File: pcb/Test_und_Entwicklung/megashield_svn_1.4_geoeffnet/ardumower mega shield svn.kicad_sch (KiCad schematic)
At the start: 21 parts, among them K3 RELAY_2RT, P16 RPI Backup P., P17 RPI Main P., P42 Charger, P43 Battery, P49 MotorStop, Q1 BC847B

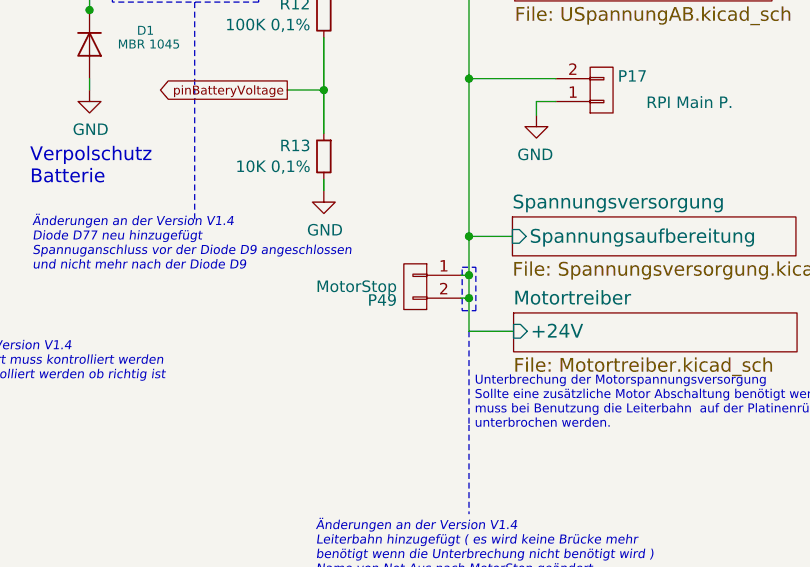
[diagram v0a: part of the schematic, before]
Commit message: megashield_svn_1.4_geoeffnet
megashield_svn_1.4_geoeffnet
23 Dioden und Mosfet unten rechts neu angeordnet
und Motorschutz Klemme von der Rückseite auf die Vorderseite umgeändert
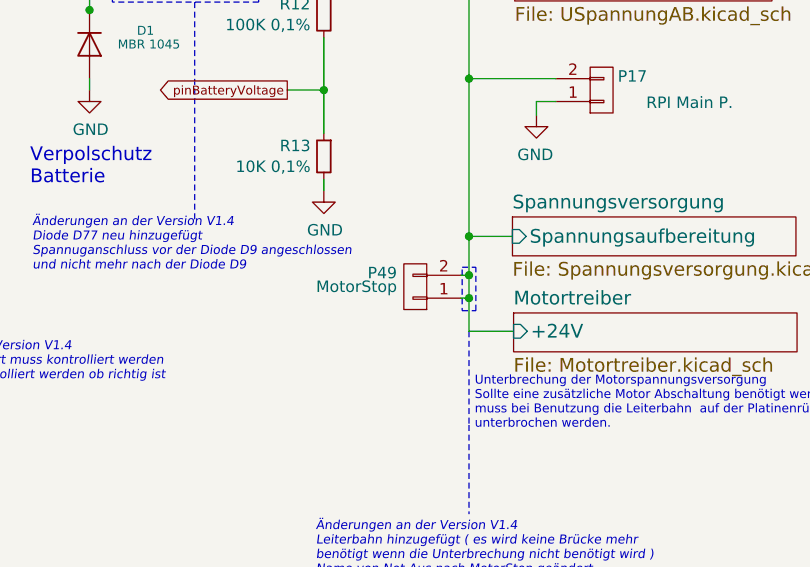
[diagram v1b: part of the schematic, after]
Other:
- moved on the sheet: P49
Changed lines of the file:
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@@
     )
   )
-  (symbol (lib_id "ardumower-mega-shield-svn-rescue:CONN_01X02-RESCUE-ardumower_mega_shield_svn") (at 222.885 99.695 0) (mirror y) (unit 1)
+  (symbol (lib_id "ardumower-mega-shield-svn-rescue:CONN_01X02-RESCUE-ardumower_mega_shield_svn") (at 222.885 99.695 180) (unit 1)
     (in_bom yes) (on_board yes)
-    (property "Reference" "P49" (id 0) (at 220.853 101.219 0)
+    (property "Reference" "P49" (id 0) (at 220.853 98.171 0)
       (effects (font (size 1.27 1.27)) (justify left))
     )
@@
       (effects (font (size 1.27 1.27)) (justify left))
     )
-    (property "Footprint" "Terminal_Blocks:TerminalBlock_Pheonix_MKDS1.5-2pol" (id 2) (at 227.2538 96.4438 90)
+    (property "Footprint" "Terminal_Blocks:TerminalBlock_Pheonix_MKDS1.5-2pol" (id 2) (at 227.2538 102.9462 90)
       (effects (font (size 1.27 1.27)) (justify left) hide)
     )
     (property "Datasheet" "" (id 3) (at 222.885 99.695 0))
-    (property "Gehäuseart" "Value" (id 4) (at 225.7298 96.4438 90)
+    (property "Gehäuseart" "Value" (id 4) (at 225.7298 102.9462 90)
       (effects (font (size 1.524 1.524)) (justify left) hide)
     )
-    (property "Bestelllink" "Value" (id 5) (at 227.076 96.4438 90)
+    (property "Bestelllink" "Value" (id 5) (at 227.076 102.9462 90)
       (effects (font (size 1.524 1.524)) (justify left) hide)
     )
-    (property "Technische Daten" "Value" (id 6) (at 228.4222 96.4438 90)
+    (property "Technische Daten" "Value" (id 6) (at 228.4222 102.9462 90)
       (effects (font (size 1.524 1.524)) (justify left) hide)
     )

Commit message: megashield_svn_1.4_geoeffnet
megashield_svn_1.4_geoeffnet
24 INA Neu verdrahtet und Widerstandswerte von den INA ausgetauscht
Berechnung hinzugefügt
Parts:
- R10, R13: JLCPCB LCSC Part (none) -> C95519
- R12, R9: JLCPCB LCSC Part (none) -> C95527
- R18: JLCPCB LCSC Part (none) -> C4190
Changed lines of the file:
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@@
   (title_block
     (title "Ardumower shield SVN Version")
-    (date "2020-12-30")
+    (date "2021-01-04")
     (rev "1.4")
     (company "ML AG JL UZ")
@@
       (effects (font (size 1.27 1.27)) hide)
     )
+    (property "JLCPCB LCSC Part" "C95527" (id 6) (at 111.76 62.484 0)
+      (effects (font (size 1.27 1.27)) hide)
+    )
   )
   (symbol (lib_id "ardumower-mega-shield-svn-rescue:R_Small-RESCUE-ardumower_mega_shield_svn") (at 111.76 78.232 0) (mirror y) (unit 1)
@@
       (effects (font (size 1.27 1.27)) hide)
     )
+    (property "JLCPCB LCSC Part" "C95519" (id 6) (at 111.76 78.232 0)
+      (effects (font (size 1.27 1.27)) hide)
+    )
   )
   (symbol (lib_id "ardumower-mega-shield-svn-rescue:R_Small-RESCUE-ardumower_mega_shield_svn") (at 133.858 99.568 90) (mirror x) (unit 1)
@@
       (effects (font (size 1.27 1.27)) hide)
     )
+    (property "JLCPCB LCSC Part" "C4190" (id 6) (at 133.858 99.568 0)
+      (effects (font (size 1.27 1.27)) hide)
+    )
   )
   (symbol (lib_id "ardumower-mega-shield-svn-rescue:R_Small-RESCUE-ardumower_mega_shield_svn") (at 212.725 69.469 0) (mirror y) (unit 1)
@@
       (effects (font (size 1.27 1.27)) hide)
     )
+    (property "JLCPCB LCSC Part" "C95527" (id 6) (at 212.725 69.469 0)
+      (effects (font (size 1.27 1.27)) hide)
+    )
   )
   (symbol (lib_id "ardumower-mega-shield-svn-rescue:R_Small-RESCUE-ardumower_mega_shield_svn") (at 212.725 85.217 0) (mirror y) (unit 1)
@@
       (effects (font (size 1.27 1.27)) hide)
     )
+    (property "JLCPCB LCSC Part" "C95519" (id 6) (at 212.725 85.217 0)
+      (effects (font (size 1.27 1.27)) hide)
+    )
   )
   (symbol (lib_id "ardumower-mega-shield-svn-rescue:F_10A-RESCUE-ardumower_mega_shield_svn") (at 52.197 51.816 180) (unit 1)
@@
       (reference "JP16") (unit 1) (value "5A") (footprint "Zimprich:SJ")
     )
-    (path "/882f13dd-ef74-41f9-a374-92f084b19f4e/00000000-0000-0000-0000-0000587a79b6"
-      (reference "R138") (unit 1) (value "10K") (footprint "Zimprich:R_0603")
-    )
     (path "/882f13dd-ef74-41f9-a374-92f084b19f4e/00000000-0000-0000-0000-0000587a6b3f"
-      (reference "R139") (unit 1) (value "10K") (footprint "Zimprich:R_0603")
+      (reference "R138") (unit 1) (value "6,80K") (footprint "Zimprich:R_0603")
+    )
+    (path "/882f13dd-ef74-41f9-a374-92f084b19f4e/00000000-0000-0000-0000-0000587a79b6"
+      (reference "R139") (unit 1) (value "3,30K") (footprint "Zimprich:R_0603")
     )
     (path "/882f13dd-ef74-41f9-a374-92f084b19f4e/00000000-0000-0000-0000-0000587a7cc4"
-      (reference "R140") (unit 1) (value "0.1 1% 2W") (footprint "Resistor_SMD:R_2512_6332Metric")
+      (reference "R140") (unit 1) (value "0.05 1% 2W") (footprint "Resistor_SMD:R_2512_6332Metric")
     )
   )

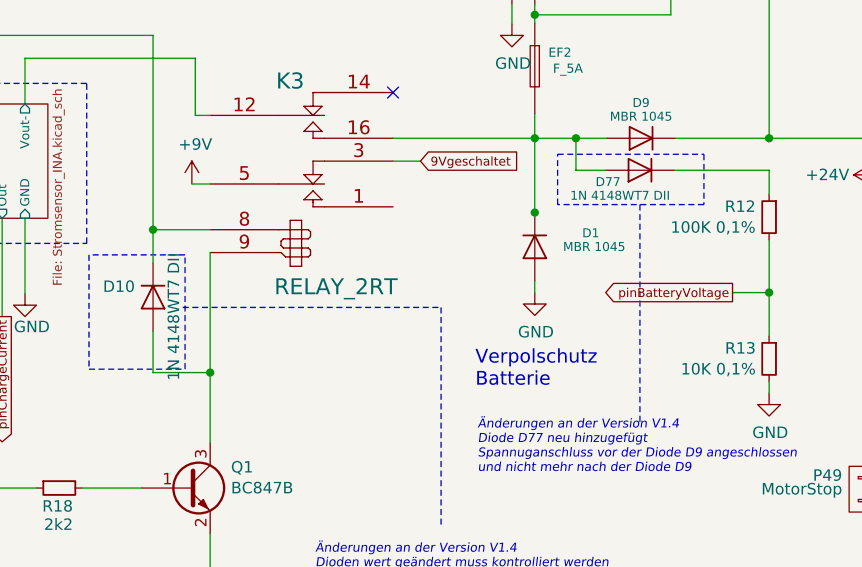
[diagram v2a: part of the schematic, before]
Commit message: megashield_svn_1.4_geoeffnet
megashield_svn_1.4_geoeffnet
26 Diode D10&D77 von Footprint SOD-523 auf SOD-123 & auf 1N4148W geändert
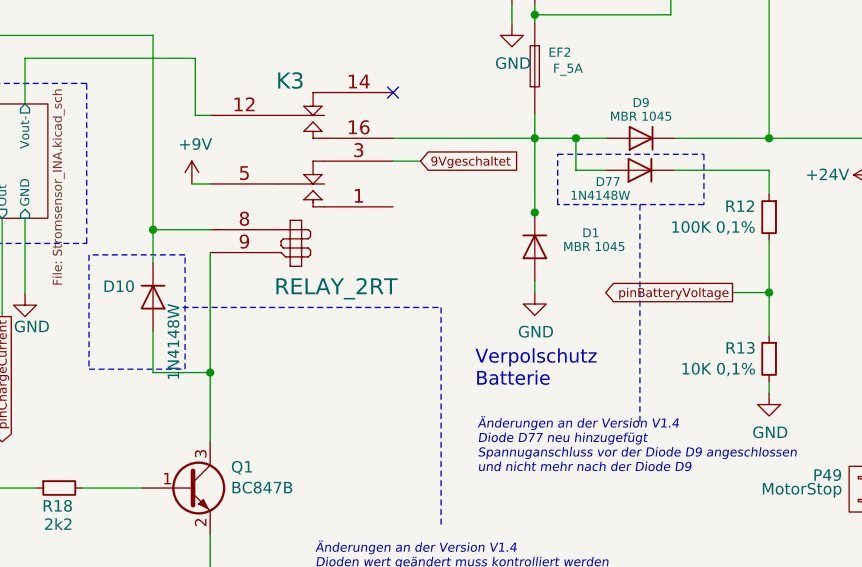
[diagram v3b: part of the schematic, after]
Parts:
- D10: value 1N 4148WT7 DII -> 1N4148W; footprint Diode_SMD:D_SOD-523 -> Diode_SMD:D_SOD-123; Bauform SOD-523 -> SOD-123; Bestelllink https://www.reichelt.de/schalt-diode-100-v-150-ma-sod-523-1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 -> https://www.reichelt.de/schalt-diode-75-v-150-ma-sod-123-rn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; Bestellnummer R: 1N 4148WT7 DII -> R: RND 1N4148W; Funktion Schalt-Diode, 100 V, 150 mA, SOD-523 -> Schalt-Diode, 75 V, 150 mA, SOD-123; Gehäuseart SOD-523 -> SOD-123; Reichelt-Bestellnummer R: 1N 4148WT7 DII -> R: RND 1N4148W; Technische Daten Schalt-Diode, 100 V, 150 mA, SOD-523 -> Schalt-Diode, 75 V, 150 mA, SOD-123
- D77: value 1N 4148WT7 DII -> 1N4148W; footprint Diode_SMD:D_SOD-523 -> Diode_SMD:D_SOD-123; Bauform SOD-523 -> SOD-123; Bestelllink https://www.reichelt.de/schalt-diode-100-v-150-ma-sod-523-1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 -> https://www.reichelt.de/schalt-diode-75-v-150-ma-sod-123-rn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; Bestellnummer R: 1N 4148WT7 DII -> R: RND 1N4148W; Funktion Schalt-Diode, 100 V, 150 mA, SOD-523 -> Schalt-Diode, 75 V, 150 mA, SOD-123; Gehäuseart SOD-523 -> SOD-123; Hersteller Bestellnummer Value -> (none); Reichelt-Bestellnummer R: 1N 4148WT7 DII -> R: RND 1N4148W; Technische Daten Schalt-Diode, 100 V, 150 mA, SOD-523 -> Schalt-Diode, 75 V, 150 mA, SOD-123
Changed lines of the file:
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@@
   (title_block
     (title "Ardumower shield SVN Version")
-    (date "2021-01-04")
+    (date "2021-01-06")
     (rev "1.4")
     (company "ML AG JL UZ")
@@
       (effects (font (size 1.27 1.27)) (justify right))
     )
-    (property "Value" "1N 4148WT7 DII" (id 1) (at 146.5834 87.63 0)
+    (property "Value" "1N4148W" (id 1) (at 146.5834 87.63 0)
       (effects (font (size 1.27 1.27)) (justify right))
     )
-    (property "Footprint" "Diode_SMD:D_SOD-523" (id 2) (at 139.827 78.359 0)
-      (effects (font (size 1.27 1.27)) hide)
-    )
-    (property "Datasheet" "https://cdn-reichelt.de/documents/datenblatt/A400/1N4148WT_ENG_TDS.pdf" (id 3) (at 144.272 78.359 0)
-      (effects (font (size 1.27 1.27)) hide)
-    )
-    (property "Bauform" "SOD-523" (id 4) (at 144.272 78.359 0)
-      (effects (font (size 1.27 1.27)) hide)
-    )
-    (property "Bestelllink" "https://www.reichelt.de/schalt-diode-100-v-150-ma-sod-523-1n-4148wt7-dii-p219386.html?&trstct=pos_6&nbc=1" (id 5) (at 144.272 78.359 0)
-      (effects (font (size 1.27 1.27)) hide)
-    )
-    (property "Technische Daten" "Schalt-Diode, 100 V, 150 mA, SOD-523" (id 6) (at 144.272 78.359 0)
-      (effects (font (size 1.27 1.27)) hide)
-    )
-    (property "Bestellnummer" "R: 1N 4148WT7 DII" (id 7) (at 144.272 78.359 0)
-      (effects (font (size 1.27 1.27)) hide)
-    )
-    (property "Funktion" "Schalt-Diode, 100 V, 150 mA, SOD-523" (id 4) (at 144.272 78.359 0)
-      (effects (font (size 1.27 1.27)) hide)
-    )
-    (property "Gehäuseart" "SOD-523" (id 5) (at 144.272 78.359 0)
-      (effects (font (size 1.27 1.27)) hide)
-    )
-    (property "Reichelt-Bestellnummer" "R: 1N 4148WT7 DII" (id 6) (at 144.272 78.359 0)
+    (property "Footprint" "Diode_SMD:D_SOD-123" (id 2) (at 139.827 78.359 0)
+      (effects (font (size 1.27 1.27)) hide)
+    )
+    (property "Datasheet" "https://cdn-reichelt.de/documents/datenblatt/A200/RND_1N4148W_DB-EN.pdf" (id 3) (at 144.272 78.359 0)
+      (effects (font (size 1.27 1.27)) hide)
+    )
+    (property "Bauform" "SOD-123" (id 4) (at 144.272 78.359 0)
+      (effects (font (size 1.27 1.27)) hide)
+    )
+    (property "Bestelllink" "https://www.reichelt.de/schalt-diode-75-v-150-ma-sod-123-rnd-1n4148w-p223369.html?&trstct=pos_0&nbc=1" (id 5) (at 144.272 78.359 0)
+      (effects (font (size 1.27 1.27)) hide)
+    )
+    (property "Technische Daten" "Schalt-Diode, 75 V, 150 mA, SOD-123" (id 6) (at 144.272 78.359 0)
+      (effects (font (size 1.27 1.27)) hide)
+    )
+    (property "Bestellnummer" "R: RND 1N4148W" (id 7) (at 144.272 78.359 0)
+      (effects (font (size 1.27 1.27)) hide)
+    )
+    (property "Funktion" "Schalt-Diode, 75 V, 150 mA, SOD-123" (id 4) (at 144.272 78.359 0)
+      (effects (font (size 1.27 1.27)) hide)
+    )
+    (property "Gehäuseart" "SOD-123" (id 5) (at 144.272 78.359 0)
+      (effects (font (size 1.27 1.27)) hide)
+    )
+    (property "Reichelt-Bestellnummer" "R: RND 1N4148W" (id 6) (at 144.272 78.359 0)
       (effects (font (size 1.27 1.27)) hide)
     )
@@
       (effects (font (size 0.991 0.991)) (justify right))
     )
-    (property "Value" "1N 4148WT7 DII" (id 1) (at 190.627 67.081 0)
+    (property "Value" "1N4148W" (id 1) (at 190.627 67.081 0)
       (effects (font (size 0.991 0.991)) (justify right))
     )
-    (property "Footprint" "Diode_SMD:D_SOD-523" (id 2) (at 198.374 59.817 0)
-      (effects (font (size 1.27 1.27)) hide)
-    )
-    (property "Datasheet" "https://cdn-reichelt.de/documents/datenblatt/A400/1N4148WT_ENG_TDS.pdf" (id 3) (at 198.374 64.262 0)
-      (effects (font (size 1.27 1.27)) hide)
-    )
-    (property "Bauform" "SOD-523" (id 4) (at 198.374 64.262 0)
-      (effects (font (size 1.27 1.27)) hide)
-    )
-    (property "Bestelllink" "https://www.reichelt.de/schalt-diode-100-v-150-ma-sod-523-1n-4148wt7-dii-p219386.html?&trstct=pos_6&nbc=1" (id 5) (at 198.374 64.262 0)
-      (effects (font (size 1.27 1.27)) hide)
-    )
-    (property "Technische Daten" "Schalt-Diode, 100 V, 150 mA, SOD-523" (id 6) (at 198.374 64.262 0)
-      (effects (font (size 1.27 1.27)) hide)
-    )
-    (property "Bestellnummer" "R: 1N 4148WT7 DII" (id 7) (at 198.374 64.262 0)
-      (effects (font (size 1.27 1.27)) hide)
-    )
-    (property "Reichelt-Bestellnummer" "R: 1N 4148WT7 DII" (id 8) (at 198.374 64.262 0)
-      (effects (font (size 1.27 1.27)) hide)
-    )
-    (property "Funktion" "Schalt-Diode, 100 V, 150 mA, SOD-523" (id 4) (at 198.374 64.262 0)
-      (effects (font (size 1.27 1.27)) hide)
-    )
-    (property "Gehäuseart" "SOD-523 " (id 5) (at 198.374 64.262 0)
-      (effects (font (size 1.27 1.27)) hide)
-    )
-    (property "Hersteller Bestellnummer" "Value" (id 6) (at 198.374 64.262 0)
+    (property "Footprint" "Diode_SMD:D_SOD-123" (id 2) (at 198.374 59.817 0)
+      (effects (font (size 1.27 1.27)) hide)
+    )
+    (property "Datasheet" "https://cdn-reichelt.de/documents/datenblatt/A200/RND_1N4148W_DB-EN.pdf" (id 3) (at 198.374 64.262 0)
+      (effects (font (size 1.27 1.27)) hide)
+    )
+    (property "Bauform" "SOD-123" (id 4) (at 198.374 64.262 0)
+      (effects (font (size 1.27 1.27)) hide)
+    )
+    (property "Bestelllink" "https://www.reichelt.de/schalt-diode-75-v-150-ma-sod-123-rnd-1n4148w-p223369.html?&trstct=pos_0&nbc=1" (id 5) (at 198.374 64.262 0)
+      (effects (font (size 1.27 1.27)) hide)
+    )
+    (property "Technische Daten" "Schalt-Diode, 75 V, 150 mA, SOD-123" (id 6) (at 198.374 64.262 0)
+      (effects (font (size 1.27 1.27)) hide)
+    )
+    (property "Bestellnummer" "R: RND 1N4148W" (id 7) (at 198.374 64.262 0)
+      (effects (font (size 1.27 1.27)) hide)
+    )
+    (property "Reichelt-Bestellnummer" "R: RND 1N4148W" (id 8) (at 198.374 64.262 0)
+      (effects (font (size 1.27 1.27)) hide)
+    )
+    (property "Funktion" "Schalt-Diode, 75 V, 150 mA, SOD-123" (id 4) (at 198.374 64.262 0)
+      (effects (font (size 1.27 1.27)) hide)
+    )
+    (property "Gehäuseart" "SOD-123" (id 5) (at 198.374 64.262 0)
+      (effects (font (size 1.27 1.27)) hide)
+    )
+    (property "Hersteller Bestellnummer" "" (id 6) (at 198.374 64.262 0)
       (effects (font (size 1.27 1.27)) hide)
     )
@@
     )
     (path "/00000000-0000-0000-0000-000058e41856"
-      (reference "D10") (unit 1) (value "1N 4148WT7 DII") (footprint "Diode_SMD:D_SOD-523")
+      (reference "D10") (unit 1) (value "1N4148W") (footprint "Diode_SMD:D_SOD-123")
     )
     (path "/00000000-0000-0000-0000-000058915405"
@@
     )
     (path "/2f64b30b-7eec-418a-8d46-9147da41342b"
-      (reference "D77") (unit 1) (value "1N 4148WT7 DII") (footprint "Diode_SMD:D_SOD-523")
+      (reference "D77") (unit 1) (value "1N4148W") (footprint "Diode_SMD:D_SOD-123")
     )
     (path "/00000000-0000-0000-0000-000054a79b5a"

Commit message: megashield_svn_1.4_geoeffnet
megashield_svn_1.4_geoeffnet
28 Beschriftung von Deutsch auf Englisch umgeändert
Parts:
- C3, P16, P17: Bauform Value -> (none); Bestelllink Value -> (none); Funktion Value -> (none); Gehäuseart Value -> (none); Technische Daten Value -> (none)
- D1, D73, D9, Q1: Bauform Value -> (none)
- D10, D77: Bauform SOD-123 -> (none)
- EF1, EF2, EF3: Bauform Value -> (none); Gehäuseart Value -> (none)
- K3: Bestelllink (none) -> http://www.reichelt.de/Print-Steckrelais/FIN-40-52-9-6V/3/i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; Bestellnummer Siehe Bauteileigenschaften -> R: FIN 40.52.9 24V / R: FIN 40.52.9 12V / R: FIN 40.52.9 6V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; Bestellnummer 12V R: FIN 40.52.9 12V -> (none); Bestellnummer 24V R: FIN 40.52.9 24V -> (none); Bestellnummer 6V R: FIN 40.52.9 6V -> (none); Bestücken (Assemble) NEIN (NO) SolderJumper -> NEIN (NO); Quelle http://www.reichelt.de/Print-Steckrelais/FIN-40-52-9-6V/3/i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 -> (none)
- P42, P43, P49: Bauform Value -> (none); Bestelllink Value -> (none); Gehäuseart Value -> (none); Technische Daten Value -> (none)
- R10, R13: Bauform 1206 -> (none); JLCPCB LCSC Part C95519 -> (none)
- R12, R9: Bauform 1206 -> (none); JLCPCB LCSC Part C95527 -> (none)
- R18: Bauform Value -> (none); JLCPCB LCSC Part C4190 -> (none)
